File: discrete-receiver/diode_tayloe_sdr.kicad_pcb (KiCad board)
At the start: 4 copper layers, 110 x 110 mm, 267 parts, among them J2 Optional 5V DC Jack, J3 External Filter, J4 Debug Pins, J5 Display Connector, J6 SI-52003-F, T1 H1102NLT, T2 MABA-007159-000000, U1 SN74CBT3253DBQR, U10 MS5351M, U11 Ag9905LP, U13 LM66100DCK, U14 LM66100DCK, U15 LM66100DCK, U16 PSA4-5043_, U2 OPA1612AxD, U3 OPA1612AxD, U4 CJC5340, U5 ADE-1+, U6 RP2350A, U7 W25Q128, U9 LAN8720A, X1 YC24.576MUBCE2O, X2 X322512MSB4SI

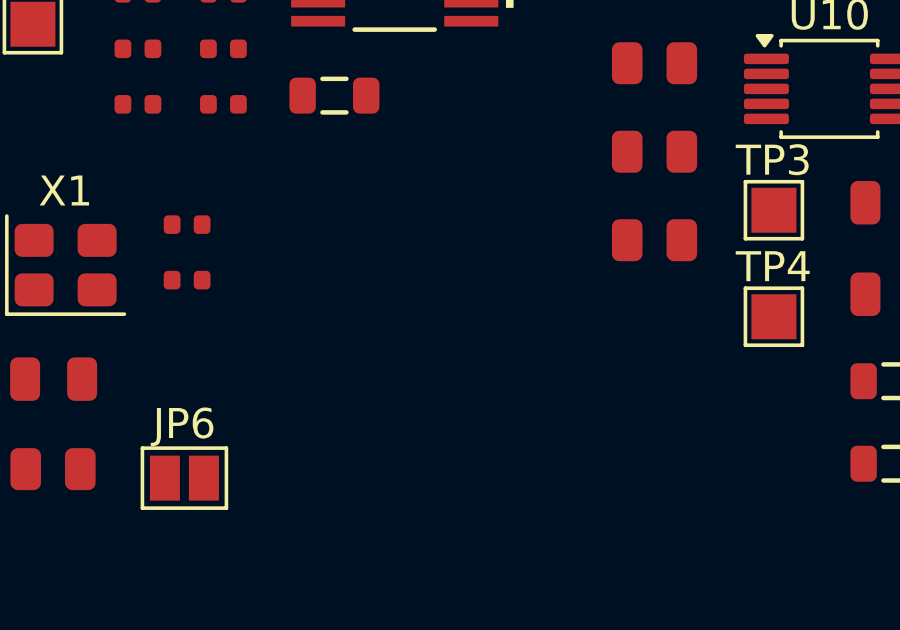
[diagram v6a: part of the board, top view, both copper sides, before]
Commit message: added L7 footprint to PCB
it was in my global library but not the local library
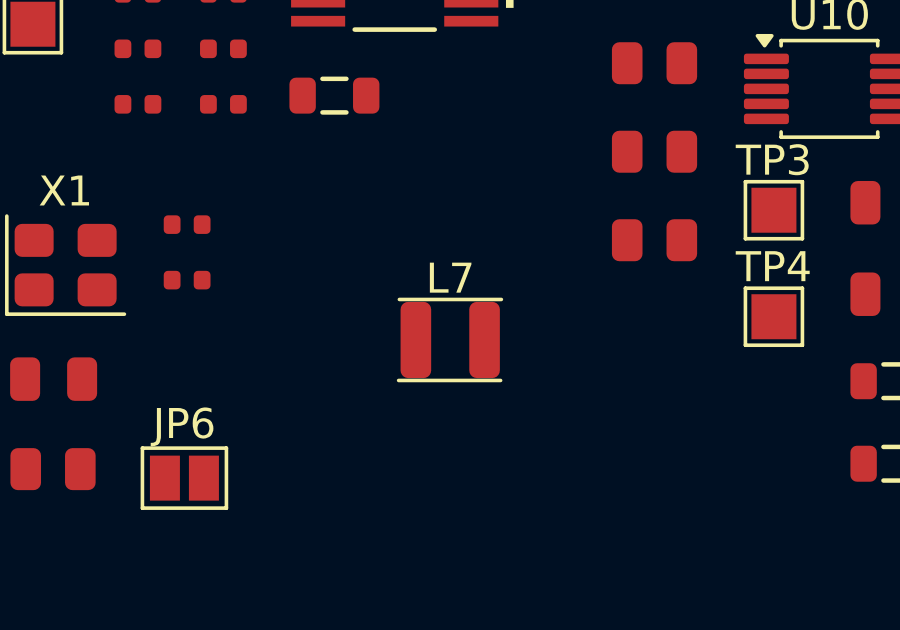
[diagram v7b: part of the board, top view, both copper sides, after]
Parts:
- added L7: 22nH, Inductor_SMD:L_APV_AHW2520, F.Cu at (196.0, 128.1)
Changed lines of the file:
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@@
 				(font
 					(size 1.27 1.27)
+					(thickness 0.15)
 				)
 			)
@@
 				(font
 					(size 1.27 1.27)
+					(thickness 0.15)
 				)
 			)
@@
 				(font
 					(size 1.27 1.27)
+					(thickness 0.15)
 				)
 			)
@@
 				(font
 					(size 1.27 1.27)
+					(thickness 0.15)
 				)
 			)
@@
 				(font
 					(size 1.27 1.27)
+					(thickness 0.15)
 				)
 			)
@@
 				(font
 					(size 1.27 1.27)
+					(thickness 0.15)
 				)
 			)
@@
 				(font
 					(size 1.27 1.27)
+					(thickness 0.15)
 				)
 			)
@@
 				(font
 					(size 1.27 1.27)
+					(thickness 0.15)
 				)
 			)
@@
 				(font
 					(size 1.27 1.27)
+					(thickness 0.15)
 				)
 			)
@@
 				(font
 					(size 1.27 1.27)
+					(thickness 0.15)
 				)
 			)
@@
 				(font
 					(size 1.27 1.27)
+					(thickness 0.15)
 				)
 			)
@@
 				(font
 					(size 1.27 1.27)
+					(thickness 0.15)
 				)
 			)
@@
 				(font
 					(size 1.27 1.27)
+					(thickness 0.15)
 				)
 			)
@@
 				(font
 					(size 1.27 1.27)
+					(thickness 0.15)
 				)
 			)
@@
 		(embedded_fonts no)
 	)
+	(footprint "Inductor_SMD:L_APV_AHW2520"
+		(layer "F.Cu")
+		(at 196.04 128.07)
+		(descr "Inductor, APV, ANR252010, 2.5x2.0x1.0mm, (http://en.apvind.com/public/upload/20240407/3375c395e460caa8519b4d637d9113ce.pdf)")
+		(tags "wirewound power shielded")
+		(property "Reference" "L7"
+			(at 0 -2.04 0)
+			(layer "F.SilkS")
+			(effects
+				(font
+					(size 1 1)
+					(thickness 0.15)
+				)
+			)
+		)
+		(property "Value" "22nH"
+			(at 0 2.05 0)
+			(layer "F.Fab")
+			(effects
+				(font
+					(size 1 1)
+					(thickness 0.15)
+				)
+			)
+		)
+		(property "Datasheet" ""
+			(at 0 0 0)
+			(layer "F.Fab")
+			(hide yes)
+			(effects
+				(font
+					(size 1.27 1.27)
+				)
+			)
+		)
+		(property "Description" "Inductor, small symbol"
+			(at 0 0 0)
+			(layer "F.Fab")
+			(hide yes)
+			(effects
+				(font
+					(size 1.27 1.27)
+				)
+			)
+		)
+		(property "KiLib_Generator" "inductor/SMD"
+			(at 0 0 0)
+			(layer "F.SilkS")
+			(hide yes)
+			(effects
+				(font
+					(size 1 1)
+					(thickness 0.15)
+				)
+			)
+		)
+		(property "LCSC" "C7427075"
+			(at 0 0 0)
+			(unlocked yes)
+			(layer "F.Fab")
+			(hide yes)
+			(effects
+				(font
+					(size 1 1)
+					(thickness 0.15)
+				)
+			)
+		)
+		(property ki_fp_filters "Choke_* *Coil* Inductor_* L_*")
+		(sheetname "/Receiver/Charles/")
+		(sheetfile "charles.kicad_sch")
+		(units
+			(unit
+				(name "A")
+				(pins "1" "2")
+			)
+		)
+		(attr smd)
+		(duplicate_pad_numbers_are_jumpers no)
+		(fp_line
+			(start -1.725 1.35)
+			(end 1.675 1.35)
+			(stroke
+				(width 0.12)
+				(type solid)
+			)
+			(layer "F.SilkS")
+		)
+		(fp_line
+			(start -1.7 -1.35)
+			(end 1.7 -1.35)
+			(stroke
+				(width 0.12)
+				(type solid)
+			)
+			(layer "F.SilkS")
+		)
+		(fp_line
+			(start -1.825 -1.35)
+			(end 1.8136 -1.35)
+			(stroke
+				(width 0.05)
+				(type solid)
+			)
+			(layer "F.CrtYd")
+		)
+		(fp_line
+			(start -1.825 1.35)
+			(end -1.825 -1.35)
+			(stroke
+				(width 0.05)
+				(type solid)
+			)
+			(layer "F.CrtYd")
+		)
+		(fp_line
+			(start -1.825 1.35)
+			(end 1.8136 1.35)
+			(stroke
+				(width 0.05)
+				(type solid)
+			)
+			(layer "F.CrtYd")
+		)
+		(fp_line
+			(start 1.815 -1.35)
+			(end 1.815 1.35)
+			(stroke
+				(width 0.05)
+				(type solid)
+			)
+			(layer "F.CrtYd")
+		)
+		(fp_rect
+			(start -1.575 -1)
+			(end 1.565 1)
+			(stroke
+				(width 0.1)
+				(type solid)
+			)
+			(fill no)
+			(layer "F.Fab")
+		)
+		(fp_text user "${REFERENCE}"
+			(at 0 0 0)
+			(layer "F.Fab")
+			(effects
+				(font
+					(size 0.62 0.62)
+					(thickness 0.09)
+				)
+			)
+		)
+		(pad "1" smd roundrect
+			(at -1.15 0)
+			(size 1.02 2.54)
+			(layers "F.Cu" "F.Mask" "F.Paste")
+			(roundrect_rratio 0.25)
+			(net "Net-(C61-Pad2)")
+			(pintype "passive")
+		)
+		(pad "2" smd roundrect
+			(at 1.14 0)
+			(size 1.02 2.54)
+			(layers "F.Cu" "F.Mask" "F.Paste")
+			(roundrect_rratio 0.25)
+			(net "Net-(C62-Pad2)")
+			(pintype "passive")
+		)
+		(embedded_fonts no)
+		(model "${KICAD10_3DMODEL_DIR}/Inductor_SMD.3dshapes/L_APV_ANR252010.step"
+			(offset
+				(xyz 0 0 0)
+			)
+			(scale
+				(xyz 1 1 1)
+			)
+			(rotate
+				(xyz 0 0 0)
+			)
+		)
+	)
 	(footprint "PCM_JLCPCB:C_0402"
 		(layer "F.Cu")
@@
 				(font
 					(size 1.27 1.27)
+					(thickness 0.15)
 				)
 			)
@@
 				(font
 					(size 1.27 1.27)
+					(thickness 0.15)
 				)
 			)
@@
 				(font
 					(size 1.27 1.27)
+					(thickness 0.15)
 				)
 			)
@@
 				(font
 					(size 1.27 1.27)
+					(thickness 0.15)
 				)
 			)
@@
 				(font
 					(size 1.27 1.27)
+					(thickness 0.15)
 				)
 			)
@@
 				(font
 					(size 1.27 1.27)
+					(thickness 0.15)
 				)
 			)
@@
 				(name "A")
 				(pins "46" "49" "50" "48" "47" "60" "56" "57" "59" "58" "55" "21" "22"
-					"2" "3" "26" "24" "25" "39" "23" "6" "54" "61" "45" "20" "38" "30" "1"
-					"11" "53" "44" "52" "51" "4" "5" "7" "8" "9" "10" "12" "13" "14" "15"
+					"2" "3" "26" "24" "25" "6" "39" "23" "54" "61" "38" "1" "20" "11" "30"
+					"45" "53" "44" "52" "51" "4" "5" "7" "8" "9" "10" "12" "13" "14" "15"
 					"16" "17" "18" "19" "27" "28" "29" "31" "32" "33" "34" "35" "36" "37"
 					"40" "41" "42" "43"
@@
 				(font
 					(size 1.27 1.27)
+					(thickness 0.15)
 				)
 			)
@@
 				(font
 					(size 1.27 1.27)
+					(thickness 0.15)
 				)
 			)
@@
 				(font
 					(size 1.27 1.27)
+					(thickness 0.15)
 				)
 			)
@@
 				(font
 					(size 1.27 1.27)
+					(thickness 0.15)
 				)
 			)
@@
 				(font
 					(size 1.27 1.27)
+					(thickness 0.15)
 				)
 			)
@@
 				(font
 					(size 1.27 1.27)
+					(thickness 0.15)
 				)
 			)
@@
 				(font
 					(size 1.27 1.27)
+					(thickness 0.15)
 				)
 			)
@@
 				(font
 					(size 1.27 1.27)
+					(thickness 0.15)
 				)
 			)
@@
 				(font
 					(size 1.27 1.27)
+					(thickness 0.15)
 				)
 			)
@@
 				(font
 					(size 1.27 1.27)
+					(thickness 0.15)
 				)
 			)

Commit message: Progress on PCB
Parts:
- moved D13 163.0 mm to (102.5, 32.8)
- moved D1 155.3 mm to (89.5, 32.5)
- moved D5 153.9 mm to (92.8, 32.5)
- moved D6 152.7 mm to (96.0, 32.5)
- moved D7 151.5 mm to (99.3, 32.5)
- moved R11 33.5 mm to (226.5, 142.8)
- moved R12 30.4 mm to (226.2, 141.5)
- moved USB1 16.2 mm to (112.5, 35.5)
- moved RF2 13.6 mm to (87.5, 134.5)
- moved RF1 6.16 mm to (119.4, 134.5)
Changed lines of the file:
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@@
 	(footprint "PCM_JLCPCB:R_0402"
 		(layer "F.Cu")
-		(at 227.195 111.075)
+		(at 226.25 141.5)
 		(descr "Resistor SMD 0402 (1005 Metric), square (rectangular) end terminal, IPC_7351 nominal, (Body size source: IPC-SM-782 page 72, https://www.pcb-3d.com/wordpress/wp-content/uploads/ipc-sm-782a_amendment_1_and_2.pdf), generated with kicad-footprint-generator")
 		(tags "resistor")
@@
 	(footprint "PCM_JLCPCB:D_0603"
 		(layer "F.Cu")
-		(at 222.135 118.525)
+		(at 96 32.5)
 		(descr "LED SMD 0603 (1608 Metric), square (rectangular) end terminal, IPC_7351 nominal, (Body size source: http://www.tortai-tech.com/upload/download/2011102023233369053.pdf), generated with kicad-footprint-generator")
 		(tags "LED")
@@
 	(footprint "PCM_JLCPCB:D_0603"
 		(layer "F.Cu")
-		(at 222.135 115.915)
+		(at 92.79 32.5)
 		(descr "LED SMD 0603 (1608 Metric), square (rectangular) end terminal, IPC_7351 nominal, (Body size source: http://www.tortai-tech.com/upload/download/2011102023233369053.pdf), generated with kicad-footprint-generator")
 		(tags "LED")
@@
 	(footprint "PCM_JLCPCB:D_0603"
 		(layer "F.Cu")
-		(at 222.135 121.135)
+		(at 99.29 32.5)
 		(descr "LED SMD 0603 (1608 Metric), square (rectangular) end terminal, IPC_7351 nominal, (Body size source: http://www.tortai-tech.com/upload/download/2011102023233369053.pdf), generated with kicad-footprint-generator")
 		(tags "LED")
@@
 	(footprint "EasyEDA_Lib:BNC-TH_DOSIN-801-0051"
 		(layer "F.Cu")
-		(at 101.014967 135.468217 -90)
+		(at 87.491009 134.457368 -90)
 		(property "Reference" "RF2"
 			(at 8.531783 -6.2005 90)
@@
 	(footprint "EasyEDA_Lib:USB-C-SMD_TYPE-C16PIN_C668624"
 		(layer "F.Cu")
-		(at 96.32 35.524 180)
+		(at 112.5 35.524 180)
 		(property "Reference" "USB1"
 			(at 0 -3.9125 0)
@@
 	(footprint "PCM_JLCPCB:R_0402"
 		(layer "F.Cu")
-		(at 227.195 109.225)
+		(at 226.5 142.75)
 		(descr "Resistor SMD 0402 (1005 Metric), square (rectangular) end terminal, IPC_7351 nominal, (Body size source: IPC-SM-782 page 72, https://www.pcb-3d.com/wordpress/wp-content/uploads/ipc-sm-782a_amendment_1_and_2.pdf), generated with kicad-footprint-generator")
 		(tags "resistor")
@@
 	(footprint "PCM_JLCPCB:D_0805"
 		(layer "F.Cu")
-		(at 243.355 114.685)
+		(at 102.5 32.75)
 		(descr "LED SMD 0805 (2012 Metric), square (rectangular) end terminal, IPC_7351 nominal, (Body size source: https://docs.google.com/spreadsheets/d/1BsfQQcO9C6DZCsRaXUlFlo91Tg2WpOkGARC1WS5S8t0/edit?usp=sharing), generated with kicad-footprint-generator")
 		(tags "LED")
@@
 	(footprint "EasyEDA_Lib:BNC-TH_DOSIN-801-0051"
 		(layer "F.Cu")
-		(at 125.514967 135.468217 -90)
+		(at 119.432568 134.468217 -90)
 		(property "Reference" "RF1"
 			(at 8.531783 -6.2005 90)
@@
 	(footprint "PCM_JLCPCB:D_0603"
 		(layer "F.Cu")
-		(at 222.135 113.305)
+		(at 89.5 32.5)
 		(descr "LED SMD 0603 (1608 Metric), square (rectangular) end terminal, IPC_7351 nominal, (Body size source: http://www.tortai-tech.com/upload/download/2011102023233369053.pdf), generated with kicad-footprint-generator")
 		(tags "LED")
